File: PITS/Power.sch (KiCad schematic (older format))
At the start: 23 parts, among them Q1 Q_PMOS_DGS, Q2 BC557, Q3 BC557, U5 LTC3112

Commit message: board - not finished
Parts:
- C11, C12, C13, C15, C16, C3, C9: footprint Capacitors_SMD:C_0805_HandSoldering -> Capacitors_SMD:C_0603_HandSoldering
- R10, R11, R16, R17, R18, R7, R9: footprint Resistors_SMD:R_0805_HandSoldering -> Resistors_SMD:R_0603_HandSoldering
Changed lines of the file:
@@
 F 0 "C9" H 5325 2250 50  0000 L CNN
 F 1 "100n" H 5325 2050 50  0000 L CNN
-F 2 "Capacitors_SMD:C_0805_HandSoldering" H 5338 2000 50  0001 C CNN
+F 2 "Capacitors_SMD:C_0603_HandSoldering" H 5338 2000 50  0001 C CNN
 F 3 "" H 5300 2150 50  0000 C CNN
 	1    5300 2150
@@
 F 0 "C3" H 3125 2250 50  0000 L CNN
 F 1 "100n" H 3125 2050 50  0000 L CNN
-F 2 "Capacitors_SMD:C_0805_HandSoldering" H 3138 2000 50  0001 C CNN
+F 2 "Capacitors_SMD:C_0603_HandSoldering" H 3138 2000 50  0001 C CNN
 F 3 "" H 3100 2150 50  0000 C CNN
 	1    3100 2150
@@
 F 0 "R7" V 3230 3200 50  0000 C CNN
 F 1 "1M" V 3150 3200 50  0000 C CNN
-F 2 "Resistors_SMD:R_0805_HandSoldering" V 3080 3200 50  0001 C CNN
+F 2 "Resistors_SMD:R_0603_HandSoldering" V 3080 3200 50  0001 C CNN
 F 3 "" H 3150 3200 50  0000 C CNN
 	1    3150 3200
@@
 F 0 "R9" V 3230 3400 50  0000 C CNN
 F 1 "1M" V 3150 3400 50  0000 C CNN
-F 2 "Resistors_SMD:R_0805_HandSoldering" V 3080 3400 50  0001 C CNN
+F 2 "Resistors_SMD:R_0603_HandSoldering" V 3080 3400 50  0001 C CNN
 F 3 "" H 3150 3400 50  0000 C CNN
 	1    3150 3400
@@
 F 0 "C13" H 5110 3170 50  0000 L CNN
 F 1 "22p" H 5110 3020 50  0000 L CNN
-F 2 "Capacitors_SMD:C_0805_HandSoldering" H 5100 3100 50  0001 C CNN
+F 2 "Capacitors_SMD:C_0603_HandSoldering" H 5100 3100 50  0001 C CNN
 F 3 "" H 5100 3100 50  0000 C CNN
 	1    5100 3100
@@
 F 0 "C12" H 5475 3100 50  0000 L CNN
 F 1 "680p" H 5475 2900 50  0000 L CNN
-F 2 "Capacitors_SMD:C_0805_HandSoldering" H 5488 2850 50  0001 C CNN
+F 2 "Capacitors_SMD:C_0603_HandSoldering" H 5488 2850 50  0001 C CNN
 F 3 "" H 5450 3000 50  0000 C CNN
 	1    5450 3000
@@
 F 0 "R10" V 6030 3000 50  0000 C CNN
 F 1 "10k" V 5950 3000 50  0000 C CNN
-F 2 "Resistors_SMD:R_0805_HandSoldering" V 5880 3000 50  0001 C CNN
+F 2 "Resistors_SMD:R_0603_HandSoldering" V 5880 3000 50  0001 C CNN
 F 3 "" H 5950 3000 50  0000 C CNN
 	1    5950 3000
@@
 F 0 "R17" V 6580 3550 50  0000 C CNN
 F 1 "158k" V 6500 3550 50  0000 C CNN
-F 2 "Resistors_SMD:R_0805_HandSoldering" V 6430 3550 50  0001 C CNN
+F 2 "Resistors_SMD:R_0603_HandSoldering" V 6430 3550 50  0001 C CNN
 F 3 "" H 6500 3550 50  0000 C CNN
 	1    6500 3550
@@
 F 0 "R18" V 6830 3200 50  0000 C CNN
 F 1 "10k" V 6750 3200 50  0000 C CNN
-F 2 "Resistors_SMD:R_0805_HandSoldering" V 6680 3200 50  0001 C CNN
+F 2 "Resistors_SMD:R_0603_HandSoldering" V 6680 3200 50  0001 C CNN
 F 3 "" H 6750 3200 50  0000 C CNN
 	1    6750 3200
@@
 F 0 "R16" V 6580 2850 50  0000 C CNN
 F 1 "845k" V 6500 2850 50  0000 C CNN
-F 2 "Resistors_SMD:R_0805_HandSoldering" V 6430 2850 50  0001 C CNN
+F 2 "Resistors_SMD:R_0603_HandSoldering" V 6430 2850 50  0001 C CNN
 F 3 "" H 6500 2850 50  0000 C CNN
 	1    6500 2850
@@
 F 0 "C16" H 7025 2950 50  0000 L CNN
 F 1 "47p" H 7025 2750 50  0000 L CNN
-F 2 "Capacitors_SMD:C_0805_HandSoldering" H 7038 2700 50  0001 C CNN
+F 2 "Capacitors_SMD:C_0603_HandSoldering" H 7038 2700 50  0001 C CNN
 F 3 "" H 7000 2850 50  0000 C CNN
 	1    7000 2850
@@
 F 0 "C15" H 5425 3750 50  0000 L CNN
 F 1 "22p" H 5425 3550 50  0000 L CNN
-F 2 "Capacitors_SMD:C_0805_HandSoldering" H 5438 3500 50  0001 C CNN
+F 2 "Capacitors_SMD:C_0603_HandSoldering" H 5438 3500 50  0001 C CNN
 F 3 "" H 5400 3650 50  0000 C CNN
 	1    5400 3650
@@
 F 0 "R11" V 5780 3650 50  0000 C CNN
 F 1 "10k" V 5700 3650 50  0000 C CNN
-F 2 "Resistors_SMD:R_0805_HandSoldering" V 5630 3650 50  0001 C CNN
+F 2 "Resistors_SMD:R_0603_HandSoldering" V 5630 3650 50  0001 C CNN
 F 3 "" H 5700 3650 50  0000 C CNN
 	1    5700 3650
@@
 F 0 "C11" H 2225 3350 50  0000 L CNN
 F 1 "1µ" H 2225 3150 50  0000 L CNN
-F 2 "Capacitors_SMD:C_0805_HandSoldering" H 2238 3100 50  0001 C CNN
+F 2 "Capacitors_SMD:C_0603_HandSoldering" H 2238 3100 50  0001 C CNN
 F 3 "" H 2200 3250 50  0000 C CNN
 	1    2200 3250

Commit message: first finished layout
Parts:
- removed Q2, Q3: BC557, TO_SOT_Packages_SMD:SOT-23, symbol BC557
- added Q2: Q_PNP_dual, TO_SOT_Packages_SMD:SOT-23-6_Handsoldering, symbol Q_PNP_dual
- R19, R6: footprint Resistors_SMD:R_0805_HandSoldering -> Resistors_SMD:R_0603_HandSoldering
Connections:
- net +5V: now also Q2.5 (E)
- net +5V_PSU: now also Q2.6 (E)
- net at C13.1, U5.2 (COMP): now also R10.2; no longer C12.2
- net at C13.2, R16.1, R17.2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: now also C12.1; no longer R10.1
- net at R6.1: now also Q2.1 (C), Q2.2 (B), Q2.3 (B)
- net at Q1.2 (G), R19.1: now also Q2.4 (C)
- new net: C12.2, R10.1
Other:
- moved on the sheet: C12, R10
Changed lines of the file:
@@
 LIBS:hoperf
 LIBS:ublox
+LIBS:bosch
 LIBS:PITS-cache
 EELAYER 25 0
@@
 L C C12
 U 1 1 5818C02E
+P 5950 3000
+F 0 "C12" H 5975 3100 50  0000 L CNN
+F 1 "680p" H 5975 2900 50  0000 L CNN
+F 2 "Capacitors_SMD:C_0603_HandSoldering" H 5988 2850 50  0001 C CNN
+F 3 "" H 5950 3000 50  0000 C CNN
+	1    5950 3000
+	0    1    1    0
+$EndComp
+$Comp
+L R R10
+U 1 1 5818C0E6
 P 5450 3000
-F 0 "C12" H 5475 3100 50  0000 L CNN
-F 1 "680p" H 5475 2900 50  0000 L CNN
-F 2 "Capacitors_SMD:C_0603_HandSoldering" H 5488 2850 50  0001 C CNN
+F 0 "R10" V 5530 3000 50  0000 C CNN
+F 1 "10k" V 5450 3000 50  0000 C CNN
+F 2 "Resistors_SMD:R_0603_HandSoldering" V 5380 3000 50  0001 C CNN
 F 3 "" H 5450 3000 50  0000 C CNN
 	1    5450 3000
-	0    1    1    0
-$EndComp
-$Comp
-L R R10
-U 1 1 5818C0E6
-P 5950 3000
-F 0 "R10" V 6030 3000 50  0000 C CNN
-F 1 "10k" V 5950 3000 50  0000 C CNN
-F 2 "Resistors_SMD:R_0603_HandSoldering" V 5880 3000 50  0001 C CNN
-F 3 "" H 5950 3000 50  0000 C CNN
-	1    5950 3000
 	0    1    1    0
 $EndComp
@@
 Connection ~ 2200 4400
 $Comp
-L GND #PWR032
+L GND #PWR034
 U 1 1 5818F2DE
 P 4200 4600
-F 0 "#PWR032" H 4200 4350 50  0001 C CNN
+F 0 "#PWR034" H 4200 4350 50  0001 C CNN
 F 1 "GND" H 4200 4450 50  0000 C CNN
 F 2 "" H 4200 4600 50  0000 C CNN
@@
 Connection ~ 5700 3400
 $Comp
-L +BATT #PWR033
+L +BATT #PWR035
 U 1 1 5818F561
 P 1800 2500
-F 0 "#PWR033" H 1800 2350 50  0001 C CNN
+F 0 "#PWR035" H 1800 2350 50  0001 C CNN
 F 1 "+BATT" H 1800 2640 50  0000 C CNN
 F 2 "" H 1800 2500 50  0000 C CNN
@@
 	4900 3400 5900 3400
 $Comp
-L +5V_PSU #PWR034
+L +5V_PSU #PWR036
 U 1 1 581E2E4B
 P 7500 2500
-F 0 "#PWR034" H 7500 2350 50  0001 C CNN
+F 0 "#PWR036" H 7500 2350 50  0001 C CNN
 F 1 "+5V_PSU" H 7500 2640 50  0000 C CNN
 F 2 "" H 7500 2500 50  0000 C CNN
@@
 $EndComp
 Connection ~ 7500 2700
-$Comp
-L BC557 Q2
-U 1 1 581E4236
-P 8900 3600
-F 0 "Q2" H 9100 3675 50  0000 L CNN
-F 1 "BC557" H 9100 3600 50  0000 L CNN
-F 2 "TO_SOT_Packages_SMD:SOT-23" H 9100 3525 50  0000 L CIN
-F 3 "" H 8900 3600 50  0000 L CNN
-	1    8900 3600
-	-1   0    0    1
-$EndComp
-$Comp
-L BC557 Q3
-U 1 1 581E423D
-P 9700 3600
-F 0 "Q3" H 9900 3675 50  0000 L CNN
-F 1 "BC557" H 9900 3600 50  0000 L CNN
-F 2 "TO_SOT_Packages_SMD:SOT-23" H 9900 3525 50  0000 L CIN
-F 3 "" H 9700 3600 50  0000 L CNN
-	1    9700 3600
-	1    0    0    1
-$EndComp
 $Comp
 L Q_PMOS_DGS Q1
@@
 F 0 "R6" V 8880 4150 50  0000 C CNN
 F 1 "10k" V 8800 4150 50  0000 C CNN
-F 2 "Resistors_SMD:R_0805_HandSoldering" V 8730 4150 50  0001 C CNN
+F 2 "Resistors_SMD:R_0603_HandSoldering" V 8730 4150 50  0001 C CNN
 F 3 "" H 8800 4150 50  0000 C CNN
 	1    8800 4150
@@
 F 0 "R19" V 9880 4150 50  0000 C CNN
 F 1 "47k" V 9800 4150 50  0000 C CNN
-F 2 "Resistors_SMD:R_0805_HandSoldering" V 9730 4150 50  0001 C CNN
+F 2 "Resistors_SMD:R_0603_HandSoldering" V 9730 4150 50  0001 C CNN
 F 3 "" H 9800 4150 50  0000 C CNN
 	1    9800 4150
@@
 Connection ~ 9800 3900
 $Comp
-L GND #PWR035
+L GND #PWR037
 U 1 1 581E4267
 P 8800 4400
-F 0 "#PWR035" H 8800 4150 50  0001 C CNN
+F 0 "#PWR037" H 8800 4150 50  0001 C CNN
 F 1 "GND" H 8800 4250 50  0000 C CNN
 F 2 "" H 8800 4400 50  0000 C CNN
@@
 $EndComp
 $Comp
-L GND #PWR036
+L GND #PWR038
 U 1 1 581E426D
 P 9800 4400
-F 0 "#PWR036" H 9800 4150 50  0001 C CNN
+F 0 "#PWR038" H 9800 4150 50  0001 C CNN
 F 1 "GND" H 9800 4250 50  0000 C CNN
 F 2 "" H 9800 4400 50  0000 C CNN
@@
 	8800 4400 8800 4300
 $Comp
-L +5V #PWR037
+L +5V #PWR039
 U 1 1 581E4275
 P 9800 3000
-F 0 "#PWR037" H 9800 2850 50  0001 C CNN
+F 0 "#PWR039" H 9800 2850 50  0001 C CNN
 F 1 "+5V" H 9800 3140 50  0000 C CNN
 F 2 "" H 9800 3000 50  0000 C CNN
@@
 Connection ~ 8800 3100
 $Comp
-L +5V_PSU #PWR038
+L +5V_PSU #PWR040
 U 1 1 581E427D
 P 8800 3000
-F 0 "#PWR038" H 8800 2850 50  0001 C CNN
+F 0 "#PWR040" H 8800 2850 50  0001 C CNN
 F 1 "+5V_PSU" H 8800 3140 50  0000 C CNN
 F 2 "" H 8800 3000 50  0000 C CNN
@@
 	1    0    0    -1
 $EndComp
+$Comp
+L Q_PNP_dual Q2
+U 1 1 585C40A3
+P 8900 3600
+F 0 "Q2" H 9100 3650 50  0000 L CNN
+F 1 "Q_PNP_dual" H 9100 3550 50  0000 L CNN
+F 2 "TO_SOT_Packages_SMD:SOT-23-6_Handsoldering" H 9100 3700 50  0001 C CNN
+F 3 "" H 8900 3600 50  0000 C CNN
+	1    8900 3600
+	-1   0    0    1
+$EndComp
+$Comp
+L Q_PNP_dual Q2
+U 2 1 585C4126
+P 9700 3600
+F 0 "Q2" H 9900 3650 50  0000 L CNN
+F 1 "Q_PNP_dual" H 9900 3550 50  0000 L CNN
+F 2 "TO_SOT_Packages_SMD:SOT-23-6_Handsoldering" H 9900 3700 50  0001 C CNN
+F 3 "" H 9700 3600 50  0000 C CNN
+	2    9700 3600
+	1    0    0    1
+$EndComp
 $EndSCHEMATC

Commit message: layout - work in progress
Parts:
- removed C10: 10µ, Capacitors_SMD:C_1206_HandSoldering, symbol C
- removed C11: 1µ, Capacitors_SMD:C_0603_HandSoldering, symbol C
- removed C12: 680p, Capacitors_SMD:C_0603_HandSoldering, symbol C
- removed C13: 22p, Capacitors_SMD:C_0603_HandSoldering, symbol C_Small
- removed C15: 22p, Capacitors_SMD:C_0603_HandSoldering, symbol C
- removed C16: 47p, Capacitors_SMD:C_0603_HandSoldering, symbol C
- removed C17: 47µ, Capacitors_SMD:C_1206_HandSoldering, symbol C
- removed C3, C9: 100n, Capacitors_SMD:C_0603_HandSoldering, symbol C
- removed L2: 4.7µH, Inductors:Inductor_Wurth_HCI-7040, symbol INDUCTOR
- removed R10, R11, R18: 10k, Resistors_SMD:R_0603_HandSoldering, symbol R
- removed R16: 845k, Resistors_SMD:R_0603_HandSoldering, symbol R
- removed R17: 158k, Resistors_SMD:R_0603_HandSoldering, symbol R
- removed R7, R9: 1M, Resistors_SMD:R_0603_HandSoldering, symbol R
- removed U5: LTC3112, Housings_SSOP:ETSSOP-20-1EP_4.4x6.5mm_Pitch0.65mm, symbol LTC3112
- added U5: TPS61030, power:TPS61030, symbol LM7805CT
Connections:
- net +5V_PSU: now also U5.3 (OUT)
- net +BATT: now also U5.1 (IN)
- net GND: now also U5.2 (GND)

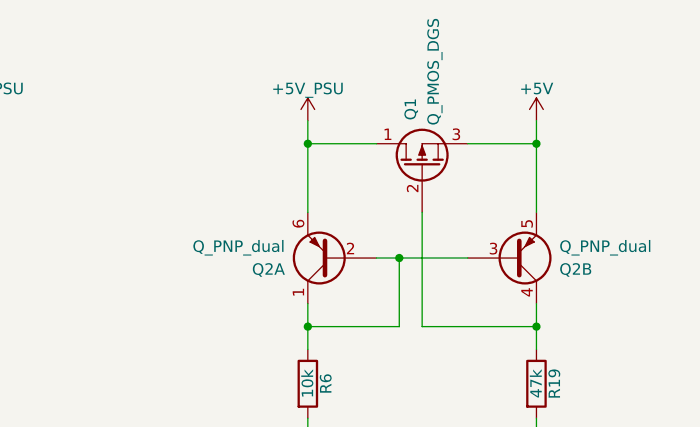
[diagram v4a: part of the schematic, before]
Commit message: ADC, BME280 and power switch
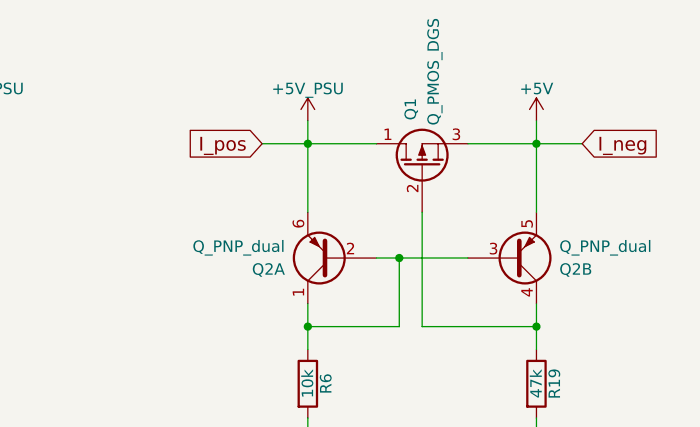
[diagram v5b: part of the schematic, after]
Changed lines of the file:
@@
 $EndDescr
 $Comp
-L +5V_PSU #PWR032
+L +5V_PSU #PWR031
 U 1 1 581E2E4B
 P 7400 3000
-F 0 "#PWR032" H 7400 2850 50  0001 C CNN
+F 0 "#PWR031" H 7400 2850 50  0001 C CNN
 F 1 "+5V_PSU" H 7400 3140 50  0000 C CNN
 F 2 "" H 7400 3000 50  0000 C CNN
@@
 $EndComp
 Wire Wire Line
-	9500 3100 9800 3100
+	9500 3100 10000 3100
 Wire Wire Line
 	9800 3000 9800 3400
 Wire Wire Line
-	9100 3100 8800 3100
+	8600 3100 9100 3100
 Wire Wire Line
 	8800 3000 8800 3400
@@
 Connection ~ 9800 3900
 $Comp
-L GND #PWR033
+L GND #PWR032
 U 1 1 581E4267
 P 8800 4400
-F 0 "#PWR033" H 8800 4150 50  0001 C CNN
+F 0 "#PWR032" H 8800 4150 50  0001 C CNN
 F 1 "GND" H 8800 4250 50  0000 C CNN
 F 2 "" H 8800 4400 50  0000 C CNN
@@
 $EndComp
 $Comp
-L GND #PWR034
+L GND #PWR033
 U 1 1 581E426D
 P 9800 4400
-F 0 "#PWR034" H 9800 4150 50  0001 C CNN
+F 0 "#PWR033" H 9800 4150 50  0001 C CNN
 F 1 "GND" H 9800 4250 50  0000 C CNN
 F 2 "" H 9800 4400 50  0000 C CNN
@@
 	8800 4400 8800 4300
 $Comp
-L +5V #PWR035
+L +5V #PWR034
 U 1 1 581E4275
 P 9800 3000
-F 0 "#PWR035" H 9800 2850 50  0001 C CNN
+F 0 "#PWR034" H 9800 2850 50  0001 C CNN
 F 1 "+5V" H 9800 3140 50  0000 C CNN
 F 2 "" H 9800 3000 50  0000 C CNN
@@
 Connection ~ 8800 3100
 $Comp
-L +5V_PSU #PWR036
+L +5V_PSU #PWR035
 U 1 1 581E427D
 P 8800 3000
-F 0 "#PWR036" H 8800 2850 50  0001 C CNN
+F 0 "#PWR035" H 8800 2850 50  0001 C CNN
 F 1 "+5V_PSU" H 8800 3140 50  0000 C CNN
 F 2 "" H 8800 3000 50  0000 C CNN
@@
 $EndComp
 $Comp
-L GND #PWR037
+L GND #PWR036
 U 1 1 598E0655
 P 6800 3600
-F 0 "#PWR037" H 6800 3350 50  0001 C CNN
+F 0 "#PWR036" H 6800 3350 50  0001 C CNN
 F 1 "GND" H 6800 3450 50  0000 C CNN
 F 2 "" H 6800 3600 50  0000 C CNN
@@
 $EndComp
 $Comp
-L +BATT #PWR038
+L +BATT #PWR037
 U 1 1 598E0B06
 P 6200 3000
-F 0 "#PWR038" H 6200 2850 50  0001 C CNN
+F 0 "#PWR037" H 6200 2850 50  0001 C CNN
 F 1 "+BATT" H 6200 3140 50  0000 C CNN
 F 2 "" H 6200 3000 50  0000 C CNN
@@
 Wire Wire Line
 	6200 3000 6200 3100
+Text GLabel 8600 3100 0    60   Input ~ 0
+I_pos
+Text GLabel 10000 3100 2    60   Input ~ 0
+I_neg
 $EndSCHEMATC

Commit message: Cleand up plan
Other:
- moved on the sheet: Q1, Q2A, Q2B, R19, R6, U5
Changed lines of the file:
@@
 encoding utf-8
 Sheet 2 2
-Title ""
-Date ""
+Title "UgoesSky-V3.0b-PITS"
+Date "2017-10-28"
 Rev ""
-Comp ""
+Comp "Jonas Gappert"
 Comment1 ""
 Comment2 ""
@@
 L +5V_PSU #PWR029
 U 1 1 581E2E4B
-P 7400 3000
-F 0 "#PWR029" H 7400 2850 50  0001 C CNN
-F 1 "+5V_PSU" H 7400 3140 50  0000 C CNN
-F 2 "" H 7400 3000 50  0000 C CNN
-F 3 "" H 7400 3000 50  0000 C CNN
-	1    7400 3000
+P 5000 3100
+F 0 "#PWR029" H 5000 2950 50  0001 C CNN
+F 1 "+5V_PSU" H 5000 3240 50  0000 C CNN
+F 2 "" H 5000 3100 50  0000 C CNN
+F 3 "" H 5000 3100 50  0000 C CNN
+	1    5000 3100
 	1    0    0    -1
 $EndComp
@@
 L Q_PMOS_DGS Q1
 U 1 1 581E4244
-P 9300 3200
-F 0 "Q1" H 9600 3250 50  0000 R CNN
-F 1 "Q_PMOS_DGS" H 9950 3150 50  0000 R CNN
-F 2 "TO_SOT_Packages_SMD:SOT-23_Handsoldering" H 9500 3300 50  0001 C CNN
-F 3 "" H 9300 3200 50  0000 C CNN
-	1    9300 3200
+P 6900 3300
+F 0 "Q1" H 7200 3350 50  0000 R CNN
+F 1 "Q_PMOS_DGS" H 7550 3250 50  0000 R CNN
+F 2 "TO_SOT_Packages_SMD:SOT-23_Handsoldering" H 7100 3400 50  0001 C CNN
+F 3 "" H 6900 3300 50  0000 C CNN
+	1    6900 3300
 	0    -1   -1   0
 $EndComp
 Wire Wire Line
-	9500 3100 10000 3100
-Wire Wire Line
-	9800 3000 9800 3400
-Wire Wire Line
-	8600 3100 9100 3100
-Wire Wire Line
-	8800 3000 8800 3400
-Wire Wire Line
-	9100 3600 9500 3600
-Wire Wire Line
-	9200 3600 9200 3900
-Wire Wire Line
-	9200 3900 8800 3900
-Wire Wire Line
-	8800 3800 8800 4000
-Connection ~ 9200 3600
-Wire Wire Line
-	9300 3400 9300 3900
-Wire Wire Line
-	9300 3900 9800 3900
-Wire Wire Line
-	9800 3800 9800 4000
+	7100 3200 7600 3200
+Wire Wire Line
+	7400 3100 7400 3500
+Wire Wire Line
+	6200 3200 6700 3200
+Wire Wire Line
+	6400 3100 6400 3500
+Wire Wire Line
+	6700 3700 7100 3700
+Wire Wire Line
+	6800 3700 6800 4000
+Wire Wire Line
+	6800 4000 6400 4000
+Wire Wire Line
+	6400 3900 6400 4100
+Connection ~ 6800 3700
+Wire Wire Line
+	6900 3500 6900 4000
+Wire Wire Line
+	6900 4000 7400 4000
+Wire Wire Line
+	7400 3900 7400 4100
 $Comp
 L R R6
 U 1 1 581E4257
-P 8800 4150
-F 0 "R6" V 8880 4150 50  0000 C CNN
-F 1 "10k" V 8800 4150 50  0000 C CNN
-F 2 "Resistors_SMD:R_0603_HandSoldering" V 8730 4150 50  0001 C CNN
-F 3 "" H 8800 4150 50  0000 C CNN
-	1    8800 4150
+P 6400 4250
+F 0 "R6" V 6480 4250 50  0000 C CNN
+F 1 "10k" V 6400 4250 50  0000 C CNN
+F 2 "Resistors_SMD:R_0603_HandSoldering" V 6330 4250 50  0001 C CNN
+F 3 "" H 6400 4250 50  0000 C CNN
+	1    6400 4250
 	1    0    0    -1
 $EndComp
@@
 L R R19
 U 1 1 581E425E
-P 9800 4150
-F 0 "R19" V 9880 4150 50  0000 C CNN
-F 1 "47k" V 9800 4150 50  0000 C CNN
-F 2 "Resistors_SMD:R_0603_HandSoldering" V 9730 4150 50  0001 C CNN
-F 3 "" H 9800 4150 50  0000 C CNN
-	1    9800 4150
-	1    0    0    -1
-$EndComp
-Connection ~ 8800 3900
-Connection ~ 9800 3900
+P 7400 4250
+F 0 "R19" V 7480 4250 50  0000 C CNN
+F 1 "47k" V 7400 4250 50  0000 C CNN
+F 2 "Resistors_SMD:R_0603_HandSoldering" V 7330 4250 50  0001 C CNN
+F 3 "" H 7400 4250 50  0000 C CNN
+	1    7400 4250
+	1    0    0    -1
+$EndComp
+Connection ~ 6400 4000
+Connection ~ 7400 4000
 $Comp
 L GND #PWR030
 U 1 1 581E4267
-P 8800 4400
-F 0 "#PWR030" H 8800 4150 50  0001 C CNN
-F 1 "GND" H 8800 4250 50  0000 C CNN
-F 2 "" H 8800 4400 50  0000 C CNN
-F 3 "" H 8800 4400 50  0000 C CNN
-	1    8800 4400
+P 6400 4500
+F 0 "#PWR030" H 6400 4250 50  0001 C CNN
+F 1 "GND" H 6400 4350 50  0000 C CNN
+F 2 "" H 6400 4500 50  0000 C CNN
+F 3 "" H 6400 4500 50  0000 C CNN
+	1    6400 4500
 	1    0    0    -1
 $EndComp
@@
 L GND #PWR031
 U 1 1 581E426D
-P 9800 4400
-F 0 "#PWR031" H 9800 4150 50  0001 C CNN
-F 1 "GND" H 9800 4250 50  0000 C CNN
-F 2 "" H 9800 4400 50  0000 C CNN
-F 3 "" H 9800 4400 50  0000 C CNN
-	1    9800 4400
-	1    0    0    -1
-$EndComp
-Wire Wire Line
-	9800 4400 9800 4300
-Wire Wire Line
-	8800 4400 8800 4300
+P 7400 4500
+F 0 "#PWR031" H 7400 4250 50  0001 C CNN
+F 1 "GND" H 7400 4350 50  0000 C CNN
+F 2 "" H 7400 4500 50  0000 C CNN
+F 3 "" H 7400 4500 50  0000 C CNN
+	1    7400 4500
+	1    0    0    -1
+$EndComp
+Wire Wire Line
+	7400 4500 7400 4400
+Wire Wire Line
+	6400 4500 6400 4400
 $Comp
 L +5V #PWR032
 U 1 1 581E4275
-P 9800 3000
-F 0 "#PWR032" H 9800 2850 50  0001 C CNN
-F 1 "+5V" H 9800 3140 50  0000 C CNN
-F 2 "" H 9800 3000 50  0000 C CNN
-F 3 "" H 9800 3000 50  0000 C CNN
-	1    9800 3000
-	1    0    0    -1
-$EndComp
-Connection ~ 9800 3100
-Connection ~ 8800 3100
+P 7400 3100
+F 0 "#PWR032" H 7400 2950 50  0001 C CNN
+F 1 "+5V" H 7400 3240 50  0000 C CNN
+F 2 "" H 7400 3100 50  0000 C CNN
+F 3 "" H 7400 3100 50  0000 C CNN
+	1    7400 3100
+	1    0    0    -1
+$EndComp
+Connection ~ 7400 3200
+Connection ~ 6400 3200
 $Comp
 L +5V_PSU #PWR033
 U 1 1 581E427D
-P 8800 3000
-F 0 "#PWR033" H 8800 2850 50  0001 C CNN
-F 1 "+5V_PSU" H 8800 3140 50  0000 C CNN
-F 2 "" H 8800 3000 50  0000 C CNN
-F 3 "" H 8800 3000 50  0000 C CNN
-	1    8800 3000
+P 6400 3100
+F 0 "#PWR033" H 6400 2950 50  0001 C CNN
+F 1 "+5V_PSU" H 6400 3240 50  0000 C CNN
+F 2 "" H 6400 3100 50  0000 C CNN
+F 3 "" H 6400 3100 50  0000 C CNN
+	1    6400 3100
 	1    0    0    -1
 $EndComp
@@
 L Q_PNP_dual Q2
 U 1 1 585C40A3
-P 8900 3600
-F 0 "Q2" H 9100 3650 50  0000 L CNN
-F 1 "Q_PNP_dual" H 9100 3550 50  0000 L CNN
-F 2 "TO_SOT_Packages_SMD:SOT-23-6_Handsoldering" H 9100 3700 50  0001 C CNN
-F 3 "" H 8900 3600 50  0000 C CNN
-	1    8900 3600
+P 6500 3700
+F 0 "Q2" H 6700 3750 50  0000 L CNN
+F 1 "Q_PNP_dual" H 6700 3650 50  0000 L CNN
+F 2 "TO_SOT_Packages_SMD:SOT-23-6_Handsoldering" H 6700 3800 50  0001 C CNN
+F 3 "" H 6500 3700 50  0000 C CNN
+	1    6500 3700
 	-1   0    0    1
 $EndComp
@@
 L Q_PNP_dual Q2
 U 2 1 585C4126
-P 9700 3600
-F 0 "Q2" H 9900 3650 50  0000 L CNN
-F 1 "Q_PNP_dual" H 9900 3550 50  0000 L CNN
-F 2 "TO_SOT_Packages_SMD:SOT-23-6_Handsoldering" H 9900 3700 50  0001 C CNN
-F 3 "" H 9700 3600 50  0000 C CNN
-	2    9700 3600
+P 7300 3700
+F 0 "Q2" H 7500 3750 50  0000 L CNN
+F 1 "Q_PNP_dual" H 7500 3650 50  0000 L CNN
+F 2 "TO_SOT_Packages_SMD:SOT-23-6_Handsoldering" H 7500 3800 50  0001 C CNN
+F 3 "" H 7300 3700 50  0000 C CNN
+	2    7300 3700
 	1    0    0    1
 $EndComp
@@
 L LM7805CT U5
 U 1 1 598E0500
-P 6800 3150
-F 0 "U5" H 6600 3350 50  0000 C CNN
-F 1 "TPS61030" H 6800 3350 50  0000 L CNN
-F 2 "power:TPS61030" H 6800 3250 50  0001 C CIN
-F 3 "" H 6800 3150 50  0000 C CNN
-	1    6800 3150
+P 4400 3250
+F 0 "U5" H 4200 3450 50  0000 C CNN
+F 1 "TPS61030" H 4400 3450 50  0000 L CNN
+F 2 "power:TPS61030" H 4400 3350 50  0001 C CIN
+F 3 "" H 4400 3250 50  0000 C CNN
+	1    4400 3250
 	1    0    0    -1
 $EndComp
@@
 L GND #PWR034
 U 1 1 598E0655
-P 6800 3600
-F 0 "#PWR034" H 6800 3350 50  0001 C CNN
-F 1 "GND" H 6800 3450 50  0000 C CNN
-F 2 "" H 6800 3600 50  0000 C CNN
-F 3 "" H 6800 3600 50  0000 C CNN
-	1    6800 3600
+P 4400 3700
+F 0 "#PWR034" H 4400 3450 50  0001 C CNN
+F 1 "GND" H 4400 3550 50  0000 C CNN
+F 2 "" H 4400 3700 50  0000 C CNN
+F 3 "" H 4400 3700 50  0000 C CNN
+	1    4400 3700
 	1    0    0    -1
 $EndComp
@@
 L +BATT #PWR035
 U 1 1 598E0B06
-P 6200 3000
-F 0 "#PWR035" H 6200 2850 50  0001 C CNN
-F 1 "+BATT" H 6200 3140 50  0000 C CNN
-F 2 "" H 6200 3000 50  0000 C CNN
-F 3 "" H 6200 3000 50  0000 C CNN
-	1    6200 3000
-	1    0    0    -1
-$EndComp
-Wire Wire Line
-	6200 3100 6400 3100
-Wire Wire Line
-	7200 3100 7400 3100
-Wire Wire Line
-	7400 3100 7400 3000
-Wire Wire Line
-	6800 3400 6800 3600
-Wire Wire Line
-	6200 3000 6200 3100
-Text GLabel 8600 3100 0    60   Input ~ 0
+P 3800 3100
+F 0 "#PWR035" H 3800 2950 50  0001 C CNN
+F 1 "+BATT" H 3800 3240 50  0000 C CNN
+F 2 "" H 3800 3100 50  0000 C CNN
+F 3 "" H 3800 3100 50  0000 C CNN
+	1    3800 3100
+	1    0    0    -1
+$EndComp
+Wire Wire Line
+	3800 3200 4000 3200
+Wire Wire Line
+	4800 3200 5000 3200
+Wire Wire Line
+	5000 3200 5000 3100
+Wire Wire Line
+	4400 3500 4400 3700
+Wire Wire Line
+	3800 3100 3800 3200
+Text GLabel 6200 3200 0    60   Input ~ 0
 I_pos
-Text GLabel 10000 3100 2    60   Input ~ 0
+Text GLabel 7600 3200 2    60   Input ~ 0
 I_neg
 $EndSCHEMATC
